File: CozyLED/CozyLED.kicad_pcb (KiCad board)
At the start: 2 copper layers, 64.8 x 25.7 mm, 34 parts, among them J1 Boot Option, J2 USB OTG, J3 UART, J4 JTAG, J5 RGB OUT, J6 12V Input, Q1 Q_NMOS_GDS, Q2 Q_NMOS_GDS, Q3 Q_NMOS_GDS, SW1 SW_Push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

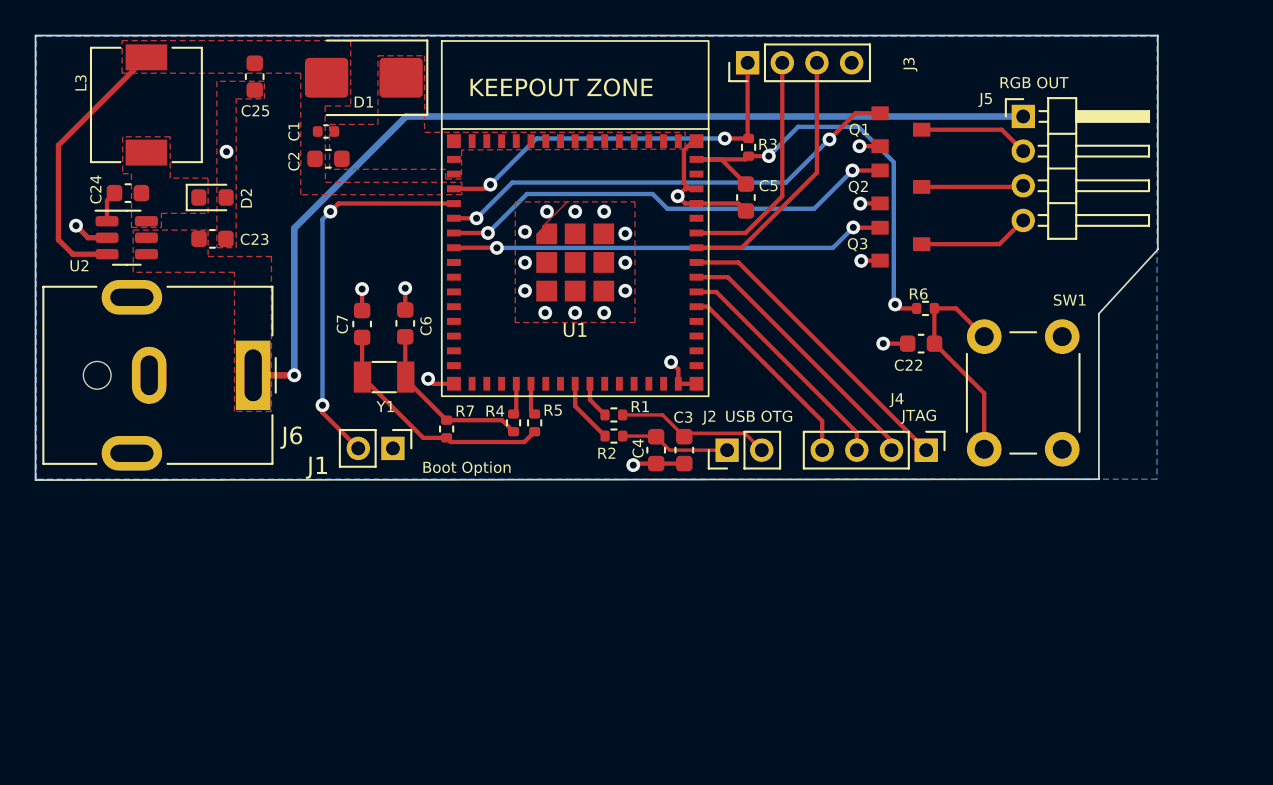
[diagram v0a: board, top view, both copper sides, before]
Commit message: Updated v0.1
- Added documentation
- Designed initial state machine
- Tested state machine to correctly initialize then enter default
- Added initial LED code for static color
- Added initial LED code for breathing color
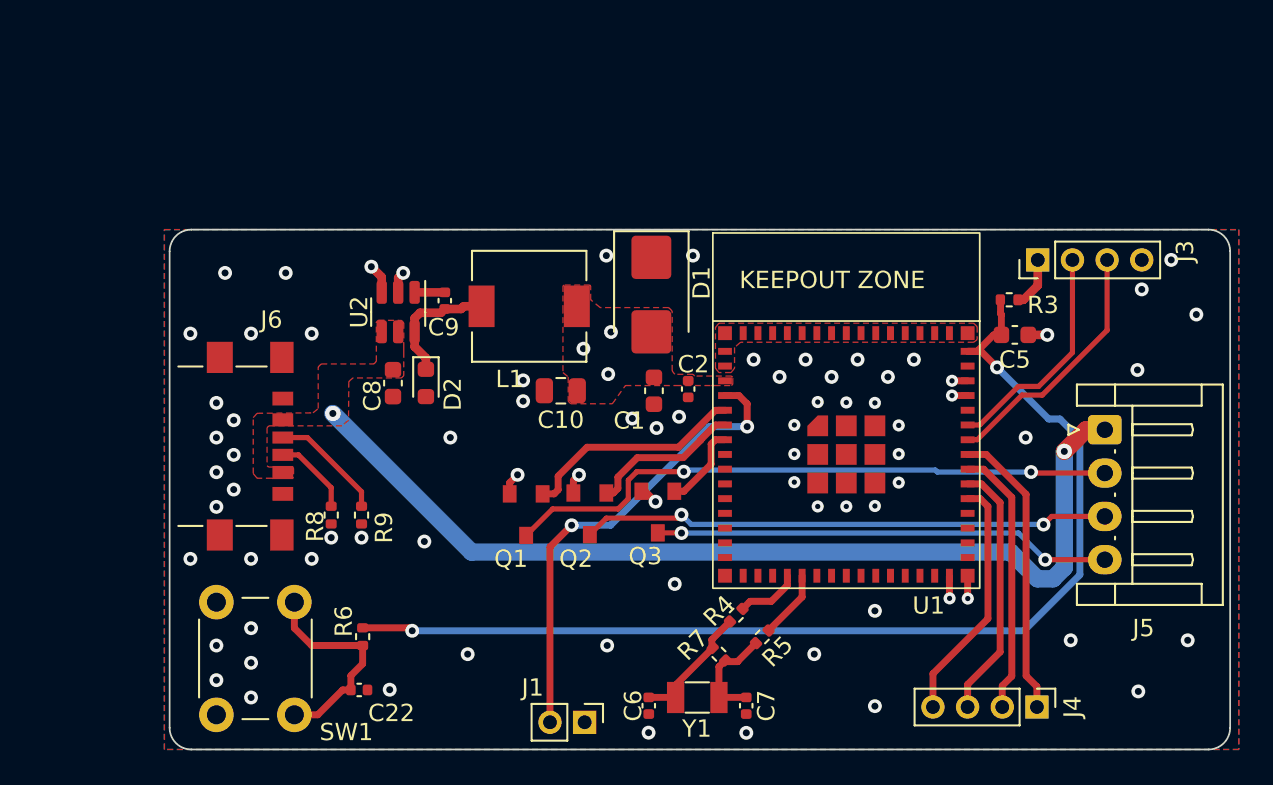
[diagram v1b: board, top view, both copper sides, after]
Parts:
- removed C23: 2.2u, Capacitor_SMD:C_0603_1608Metric
- removed C24: 100n, Capacitor_SMD:C_0603_1608Metric
- removed C25: 10u, Capacitor_SMD:C_0603_1608Metric
- removed C3, C4: TBD, Capacitor_SMD:C_0603_1608Metric
- removed J2: USB OTG, Connector_PinHeader_2.00mm:PinHeader_1x02_P2.00mm_Vertical
- removed L3: 6.8u, Inductor_SMD:L_6.3x6.3_H3
- removed R1, R2: 0, Resistor_SMD:R_0402_1005Metric
- added C10: 10u, Capacitor_SMD:C_0805_2012Metric, F.Cu at (81.9, 71.3)
- added C8: 2.2u, Capacitor_SMD:C_0603_1608Metric, F.Cu at (72.2, 70.9)
- added C9: 100n, Capacitor_SMD:C_0402_1005Metric, F.Cu at (75.2, 66.1)
- added L1: 6.8u, Inductor_SMD:L_6.3x6.3_H3, F.Cu at (80.0, 66.4)
- added R8: 5k1, Resistor_SMD:R_0402_1005Metric, F.Cu at (68.6, 78.5)
- added R9: 5k1, Resistor_SMD:R_0402_1005Metric, F.Cu at (70.4, 78.5)
- C1: footprint Capacitor_SMD:C_0402_1005Metric -> Capacitor_SMD:C_0603_1608Metric
- C2, C22, C6, C7: footprint Capacitor_SMD:C_0603_1608Metric -> Capacitor_SMD:C_0402_1005Metric
- C5: value TBD -> 1u
- J1: value Boot Option -> BOOT
- J5: footprint Connector_PinHeader_2.00mm:PinHeader_1x04_P2.00mm_Horizontal -> Connector_JST:JST_EH_S4B-EH_1x04_P2.50mm_Horizontal
- J6: value 12V Input -> USB_C_Receptacle_PowerOnly_6P; footprint Connector_BarrelJack:BarrelJack_CUI_PJ-063AH_Horizontal -> Connector_USB:USB_C_Receptacle_GCT_USB4135-GF-A_6P_TopMnt_Horizontal
- R3: value TBD -> 10k
- moved SW1 53.5 mm to (62.0, 90.0), turned to 90 degrees
- moved C22 38.1 mm to (70.2, 88.6), turned to 0 degrees
- moved R6 37.6 mm to (70.4, 85.5), turned to 90 degrees
- moved C7 31.2 mm to (92.6, 89.5), turned to -90 degrees
- moved Q1 31.0 mm to (79.9, 78.5), turned to 180 degrees
- moved C6 26.2 mm to (87.0, 89.5), turned to -90 degrees
- moved Q2 26.0 mm to (83.5, 78.4), turned to 180 degrees
- moved Y1 25.9 mm to (89.8, 89.0)
- moved C2 24.6 mm to (89.2, 71.2), turned to -90 degrees
- moved C1 24.1 mm to (87.2, 71.3), turned to -90 degrees
- moved Q3 20.9 mm to (87.5, 78.3), turned to 180 degrees
- moved D1 20.8 mm to (87.1, 65.8), turned to -90 degrees
- moved R7 20.4 mm to (91.0, 86.5), turned to 135 degrees
- moved J3 20.2 mm to (109.4, 63.8)
- moved J1 19.3 mm to (83.2, 90.4)
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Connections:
- net /RXD0 renamed /UART_RXD0
- net /TXD0 renamed /UART_TXD0
- net Net-(D2-K) renamed /LM_SW
- J5 pad 1: VCC -> +5V
- U1 pad 10: /IO6 -> unconnected-(U1B-IO6-Pad10)
- U1 pad 11: /IO7 -> unconnected-(U1B-IO7-Pad11)
- U1 pad 12: /IO8 -> unconnected-(U1B-IO8-Pad12)
- U1 pad 13: /IO9 -> unconnected-(U1B-IO9-Pad13)
- U1 pad 14: /IO10 -> unconnected-(U1B-IO10-Pad14)
- U1 pad 15: /IO11 -> unconnected-(U1B-IO11-Pad15)
- U1 pad 16: /IO12 -> unconnected-(U1B-IO12-Pad16)
- U1 pad 17: /IO13 -> unconnected-(U1B-IO13-Pad17)
- U1 pad 18: /IO14 -> unconnected-(U1B-IO14-Pad18)
- U1 pad 21: /IO17 -> unconnected-(U1B-IO17-Pad21)
- U1 pad 22: /IO18 -> unconnected-(U1B-IO18-Pad22)
- U1 pad 23: /IO19 -> unconnected-(U1B-IO19-Pad23)
- U1 pad 24: /IO20 -> unconnected-(U1B-IO20-Pad24)
- U1 pad 25: /IO21 -> unconnected-(U1B-IO21-Pad25)
- U1 pad 26: /IO26 -> unconnected-(U1B-IO26-Pad26)
- U1 pad 28: /IO33 -> unconnected-(U1B-IO33-Pad28)
- U1 pad 29: /IO34 -> unconnected-(U1B-IO34-Pad29)
- U1 pad 31: /IO35 -> unconnected-(U1B-IO35-Pad31)
- U1 pad 32: /IO36 -> unconnected-(U1B-IO36-Pad32)
- U1 pad 33: /IO37 -> unconnected-(U1B-IO37-Pad33)
- U1 pad 34: /IO38 -> unconnected-(U1B-IO38-Pad34)
- U1 pad 41: /IO45 -> unconnected-(U1B-IO45-Pad41)
- U1 pad 44: /IO46 -> unconnected-(U1B-IO46-Pad44)
- U1 pad 8: /IO4 -> unconnected-(U1B-IO4-Pad8)
- U1 pad 9: /IO5 -> unconnected-(U1B-IO5-Pad9)
- U2 pad 1: Net-(U2-CB) -> /LM_CB
- U2 pad 4: VCC -> +5V
- U2 pad 5: VCC -> +5V
- Y1 pad 1: Net-(C7-Pad1) -> Net-(C6-Pad1)
- Y1 pad 2: Net-(C6-Pad1) -> Net-(C7-Pad1)
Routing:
- net +5V: track 0.00 -> 56.0 mm, vias 0 -> 2
- net VCC: track 55.6 -> 0.00 mm, vias 1 -> 0
- net /EN: track 26.0 -> 63.6 mm
- net +3V3: track 38.2 -> 4.69 mm, vias 2 -> 4
- net /G: track 6.37 -> 35.7 mm, vias 0 -> 2
- net /R: track 5.89 -> 30.6 mm, vias 0 -> 2
- net /IO3: track 25.1 -> 4.83 mm, vias 2 -> 0
- net /B: track 6.43 -> 26.4 mm, vias 0 -> 2
- net /IO2: track 26.8 -> 8.88 mm, vias 2 -> 0
- net GND: track 28.1 -> 10.3 mm, vias 24 -> 76
- net /IO1: track 27.1 -> 13.0 mm, vias 2 -> 0
- net /USB_D+: track 9.03 -> 0.00 mm
- net Net-(C7-Pad1): track 14.0 -> 6.13 mm
- net /LM_SW: track 0.00 -> 7.37 mm
- net Net-(J6-CC1): track 0.00 -> 6.68 mm
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- added copper zone on B.Cu, net +3V3
- added copper zone on F.Cu, net +5V
- added copper zone on In1.Cu, net GND
- added copper zone on In2.Cu, net GND
- removed copper zone on F.Cu, net /LM_SW
- removed copper zone on B.Cu, net GND
- removed copper zone on F.Cu, net VCC
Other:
- board size 64.8 x 25.7 mm -> 61.2 x 30 mm
- copper layers 2 -> 4

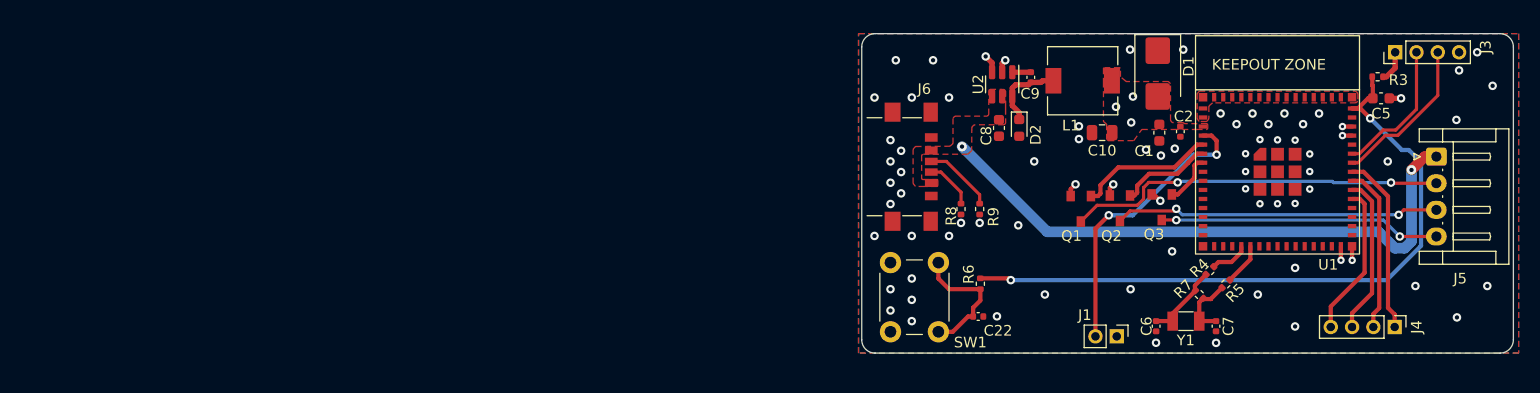
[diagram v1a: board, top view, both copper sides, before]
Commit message: Updated CozyLED PCB
Updates
- Added 12V to 3.3V sw reg (sym+footprint) with its circuitry
- Changed ESP32 symbol to S3 WROVER-E (was incorrectly S2 WROOM) with required circuitry
- Added EN&BOOT buttons
- Added breakout pins for UART, LED, and LCD
- Added nMOS transistors for RGB control (need to change source)
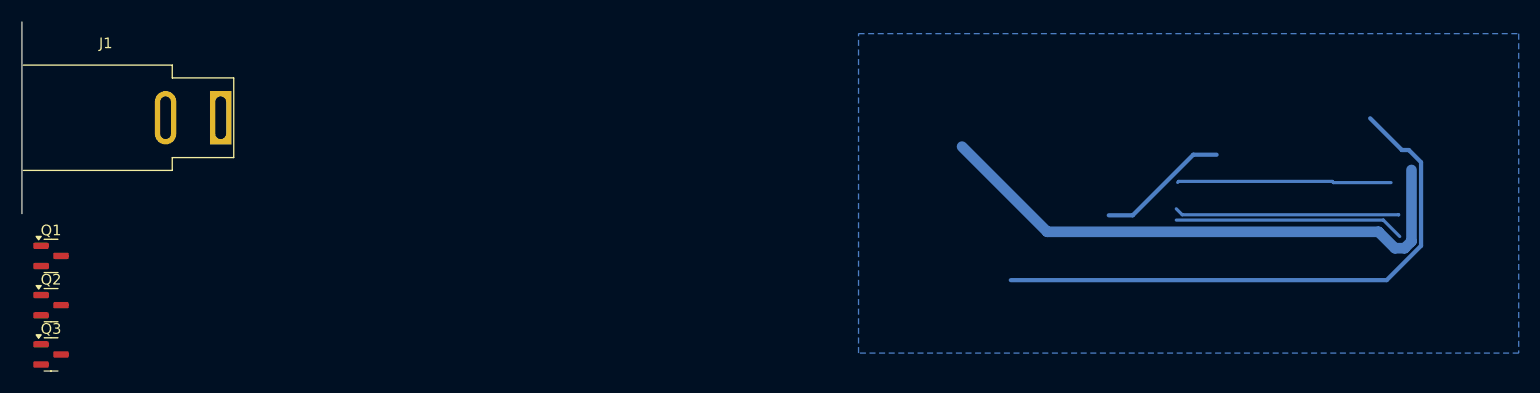
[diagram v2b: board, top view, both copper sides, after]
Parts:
- removed C1: 22p, Capacitor_SMD:C_0603_1608Metric
- removed C10: 10u, Capacitor_SMD:C_0805_2012Metric
- removed C2, C22: 0.1u, Capacitor_SMD:C_0402_1005Metric
- removed C5: 1u, Capacitor_SMD:C_0603_1608Metric
- removed C6, C7: 12p, Capacitor_SMD:C_0402_1005Metric
- removed C8: 2.2u, Capacitor_SMD:C_0603_1608Metric
- removed C9: 100n, Capacitor_SMD:C_0402_1005Metric
- removed D1: ESD, Diode_SMD:D_SMB
- removed D2: D_Schottky, Diode_SMD:D_0603_1608Metric
- removed J3: UART, Connector_PinHeader_2.00mm:PinHeader_1x04_P2.00mm_Vertical
- removed J4: JTAG, Connector_PinHeader_2.00mm:PinHeader_1x04_P2.00mm_Vertical
- removed J5: RGB OUT, Connector_JST:JST_EH_S4B-EH_1x04_P2.50mm_Horizontal
- removed J6: USB_C_Receptacle_PowerOnly_6P, Connector_USB:USB_C_Receptacle_GCT_USB4135-GF-A_6P_TopMnt_Horizontal
- removed L1: 6.8u, Inductor_SMD:L_6.3x6.3_H3
- removed R3: 10k, Resistor_SMD:R_0402_1005Metric
- removed R4, R5, R6, R7: 0, Resistor_SMD:R_0402_1005Metric
- removed R8, R9: 5k1, Resistor_SMD:R_0402_1005Metric
- removed SW1: SW_Push, Button_Switch_THT:SW_PUSH_6mm
- removed U1: ~, ESP32:ESP32_S2_MINI_2
- removed U2: LMR16006YQ3, Package_TO_SOT_SMD:SOT-23-6
- removed Y1: 32.768kHz, Crystal:Crystal_SMD_3215-2Pin_3.2x1.5mm
- J1: value BOOT -> Barrel_Jack; footprint Connector_PinHeader_2.00mm:PinHeader_1x02_P2.00mm_Vertical -> Connector_BarrelJack:BarrelJack_SwitchcraftConxall_RAPC10U_Horizontal
- Q1, Q2, Q3: value Q_NMOS_GDS -> AO3400A; footprint Diodes INC:DMN1019USN_N_CHNL -> Package_TO_SOT_SMD:SOT-23
- moved Q3 105.2 mm to (-16.8, 92.1), turned to 0 degrees
- moved Q2 100.8 mm to (-16.8, 87.5), turned to 0 degrees
- moved Q1 96.8 mm to (-16.8, 82.9), turned to 0 degrees
- moved J1 86.6 mm to (-0.90, 69.9), turned to 0 degrees
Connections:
- J1 pad 1: GND -> +12V
- J1 pad 2: /IO0 -> GND
- Q1 pad 1: /IO1 -> /GPIO_R
- Q1 pad 2: /G -> GND
- Q1 pad 3: GND -> /LED_R
- Q2 pad 1: /IO2 -> /GPIO_G
- Q2 pad 2: /R -> GND
- Q2 pad 3: GND -> /LED_G
- Q3 pad 1: /IO3 -> /GPIO_B
- Q3 pad 2: /B -> GND
- Q3 pad 3: GND -> /LED_B
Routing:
- net (no net): track 0.00 -> 182.7 mm
- net /EN: track 63.6 -> 0.00 mm, vias 2 -> 0
- net +5V: track 56.0 -> 0.00 mm, vias 2 -> 0
- net /G: track 35.7 -> 0.00 mm, vias 2 -> 0
- net /R: track 30.6 -> 0.00 mm, vias 2 -> 0
- net /IO0: track 27.2 -> 0.00 mm, vias 2 -> 0
- net /B: track 26.4 -> 0.00 mm, vias 2 -> 0
- net /IO42: track 16.9 -> 0.00 mm
- net /IO41: track 15.6 -> 0.00 mm
- net /IO40: track 14.9 -> 0.00 mm
- net /UART_TXD0: track 14.7 -> 0.00 mm
- net /IO39: track 14.3 -> 0.00 mm
- net /UART_RXD0: track 13.1 -> 0.00 mm
- net /IO1: track 13.0 -> 0.00 mm
- net Net-(C22-Pad1): track 12.6 -> 0.00 mm
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- added copper zone on B.Cu, net (none)
- removed copper zone on B.Cu, net +3V3
- removed copper zone on F.Cu, net +3V3
- removed copper zone on F.Cu, net +5V
- removed copper zone on F.Cu, net GND
- removed copper zone on In1.Cu, net GND
- removed copper zone on In2.Cu, net GND
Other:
- board outline removed

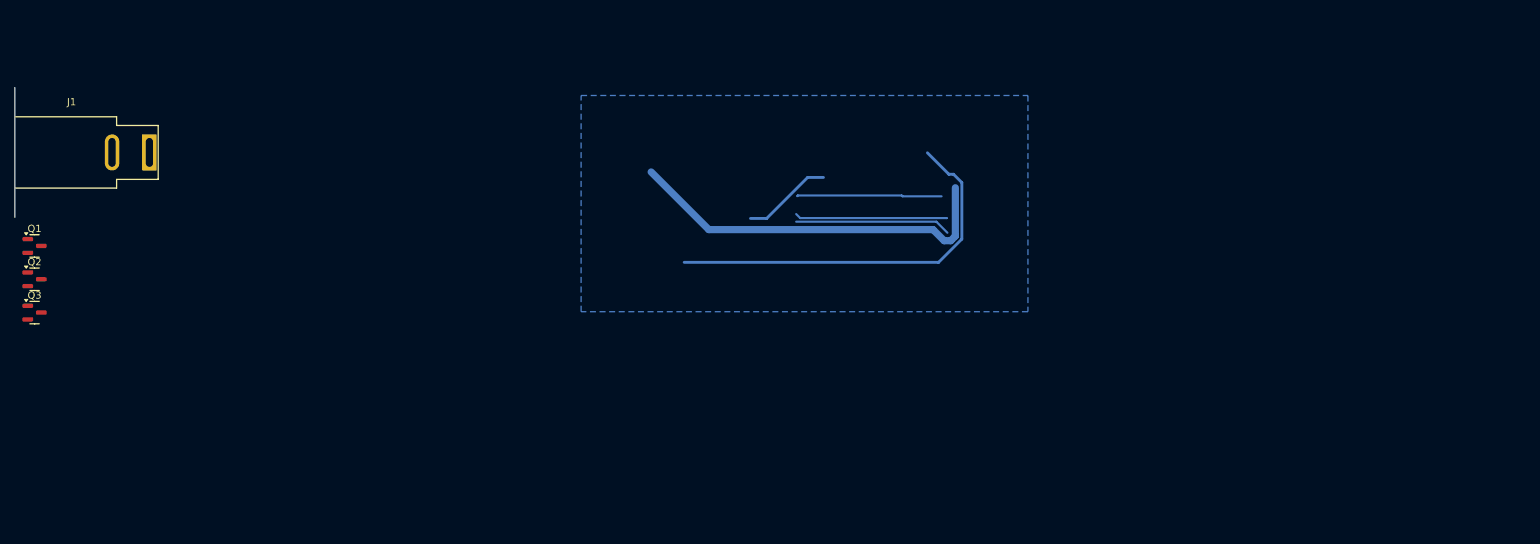
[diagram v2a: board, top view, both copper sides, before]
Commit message: Updated CozyLED schematic
Updates
- Added footprints for each component
- Added symbols, footprints, and 3D models for the DC-DC converter's components
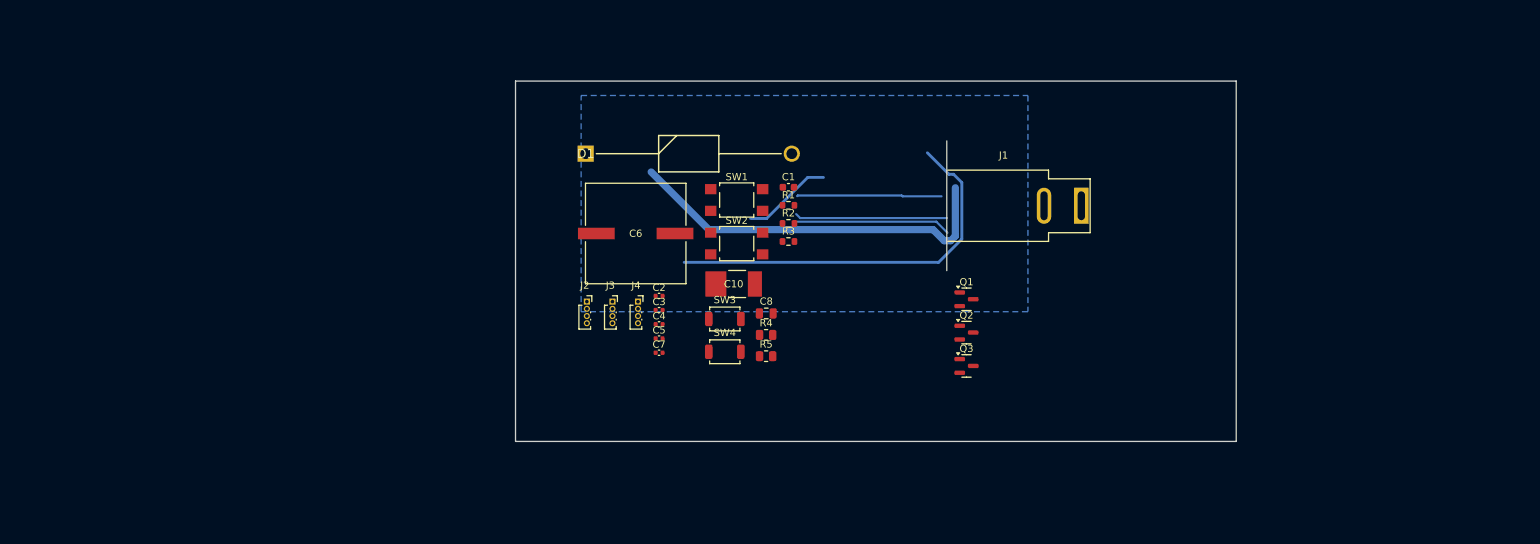
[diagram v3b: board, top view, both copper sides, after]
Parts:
- added C1: 22u, Capacitor_SMD:C_0603_1608Metric, F.Cu at (87.8, 74.7)
- added C10: 47u, Capacitor Tantalum:PCAP_594D_C_VIS, F.Cu at (80.2, 88.2)
- added C2: 0.1u, Capacitor_SMD:C_0402_1005Metric, F.Cu at (69.8, 89.8)
- added C3: 0.1u, Capacitor_SMD:C_0402_1005Metric, F.Cu at (69.8, 91.8)
- added C4: 0.1u, Capacitor_SMD:C_0402_1005Metric, F.Cu at (69.8, 93.8)
- added C5: 0.1u (NC), Capacitor_SMD:C_0402_1005Metric, F.Cu at (69.8, 95.7)
- added C6: 47u, EEVFK2A470Q, Capacitor Alum:CAP_EEFK_H13_PAN, F.Cu at (66.6, 81.2)
- added C7: 0.1u, Capacitor_SMD:C_0402_1005Metric, F.Cu at (69.8, 97.7)
- added C8: 0.1u, 0805, Capacitor_SMD:C_0805_2012Metric, F.Cu at (84.7, 92.2)
- added D1: SB5H100, Schottky Diode THT:DIOAD2855W132L835D505, F.Cu at (59.6, 70.1)
- added J2: LCD DISPLAY, Connector_PinSocket_1.00mm:PinSocket_1x04_P1.00mm_Vertical, F.Cu at (59.8, 90.6)
- added J3: LED Pins, Connector_PinSocket_1.00mm:PinSocket_1x04_P1.00mm_Vertical, F.Cu at (63.4, 90.6)
- added J4: UART, Connector_PinSocket_1.00mm:PinSocket_1x04_P1.00mm_Vertical, F.Cu at (66.9, 90.6)
- added R1: 100k, Resistor_SMD:R_0603_1608Metric, F.Cu at (87.8, 77.2)
- added R2: 100k, Resistor_SMD:R_0603_1608Metric, F.Cu at (87.8, 79.8)
- added R3: 10k, Resistor_SMD:R_0603_1608Metric, F.Cu at (87.8, 82.3)
- added R4: 1M, 0805, Resistor_SMD:R_0805_2012Metric, F.Cu at (84.7, 95.2)
- added R5: 384k, 0805, Resistor_SMD:R_0805_2012Metric, F.Cu at (84.7, 98.2)
- added SW1: LEFT, Button_Switch_SMD:SW_SPST_TL3305A, F.Cu at (80.6, 76.5)
- added SW2: RIGHT, Button_Switch_SMD:SW_SPST_TL3305A, F.Cu at (80.6, 82.5)
- added SW3: EN, Button_Switch_SMD:SW_SPST_TS-1088-xR020, F.Cu at (78.9, 93.0)
- added SW4: BOOT, Button_Switch_SMD:SW_SPST_TS-1088-xR020, F.Cu at (78.9, 97.6)
- moved J1 129.5 mm to (128.4, 77.3)
- moved Q1 129.5 mm to (112.5, 90.3)
- moved Q2 129.5 mm to (112.5, 94.9)
- moved Q3 129.5 mm to (112.5, 99.5)
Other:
- board outline added: 100 x 50 mm
